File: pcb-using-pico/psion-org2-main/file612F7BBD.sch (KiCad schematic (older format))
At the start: 39 parts, among them SW1 AC_ON, SW10 n, SW11 t, SW12 del, SW13 up, SW14 c, SW15 i, SW16 o, SW17 u, SW18 y, SW19 down, SW2 A, SW20 d, SW21 j, SW22 p, SW23 v, SW24 z, SW25 left, SW26 e, SW27 k, SW28 q, SW29 w, SW3 g, SW30 spc, SW31 right, SW32 f, SW33 L, SW34 r, SW35 x, SW36 exe, SW4 m, SW5 s, SW6 shft, SW7 mode, SW8 b, SW9 h

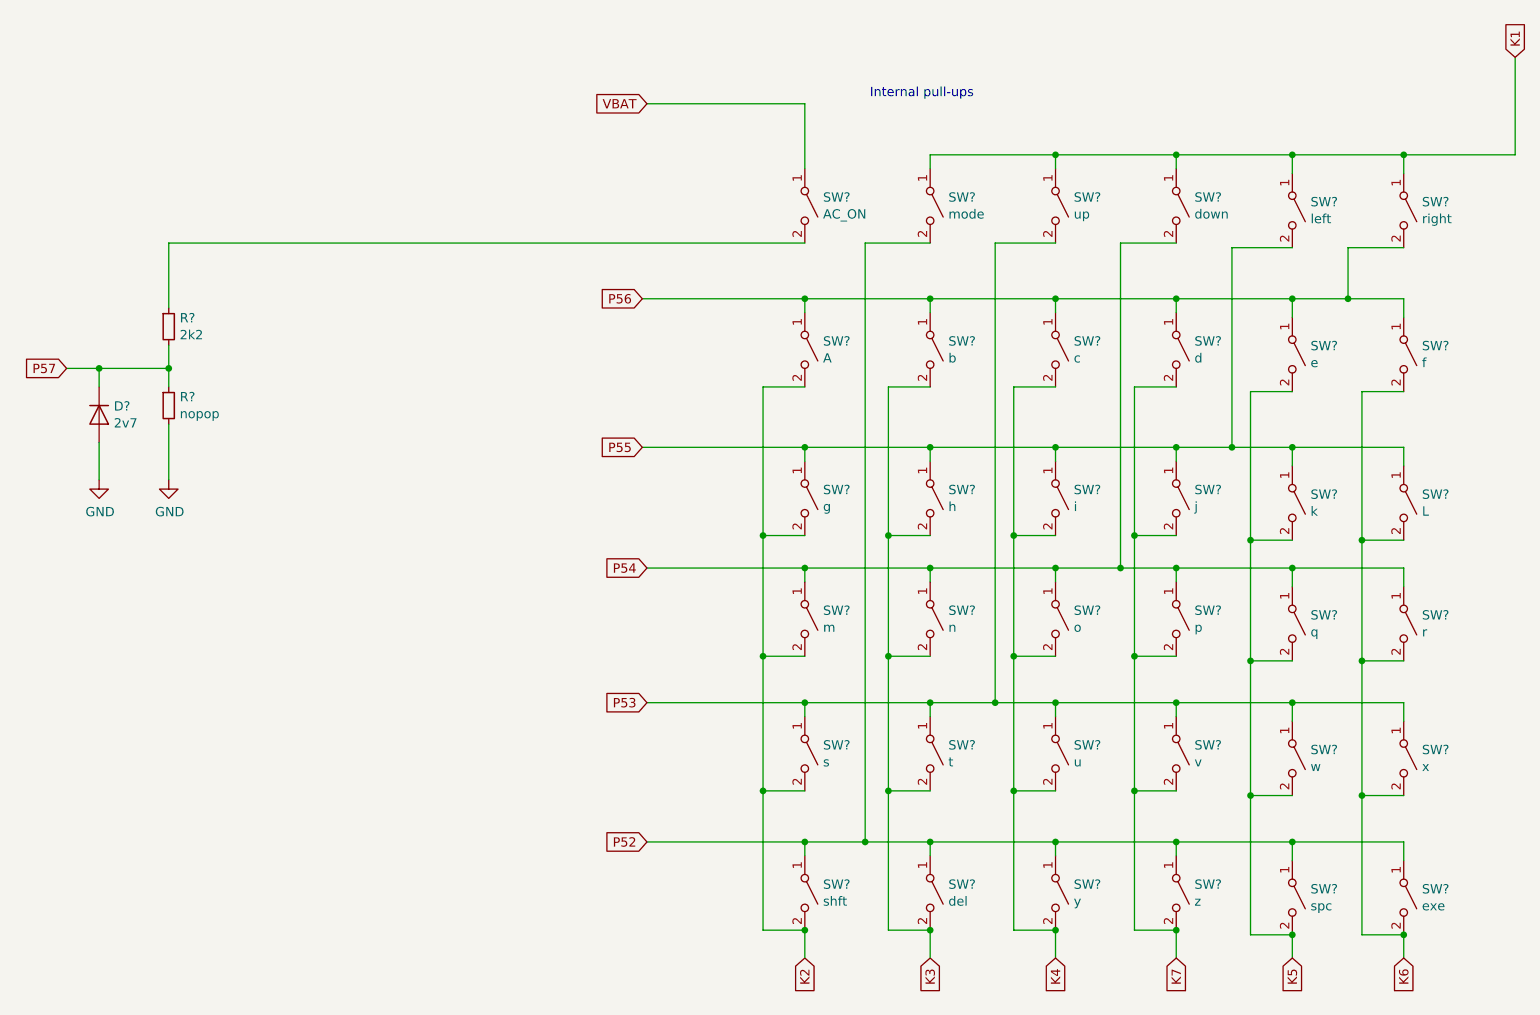
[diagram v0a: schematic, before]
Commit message: Fixed comment typo. Reverted schematic to previous version (966dcfb2f9e5fb2f0f6e9c85d958500d25748731) as a change (7bf7705c572b4e37423d66cfa6dac4b195edf464) somehow managed to create a bad hierarchical page reference for the keypad. Component designations were lost and the PCB didn't update properly. I think its all fixed now, the PCB is updated and DRC runs fine.
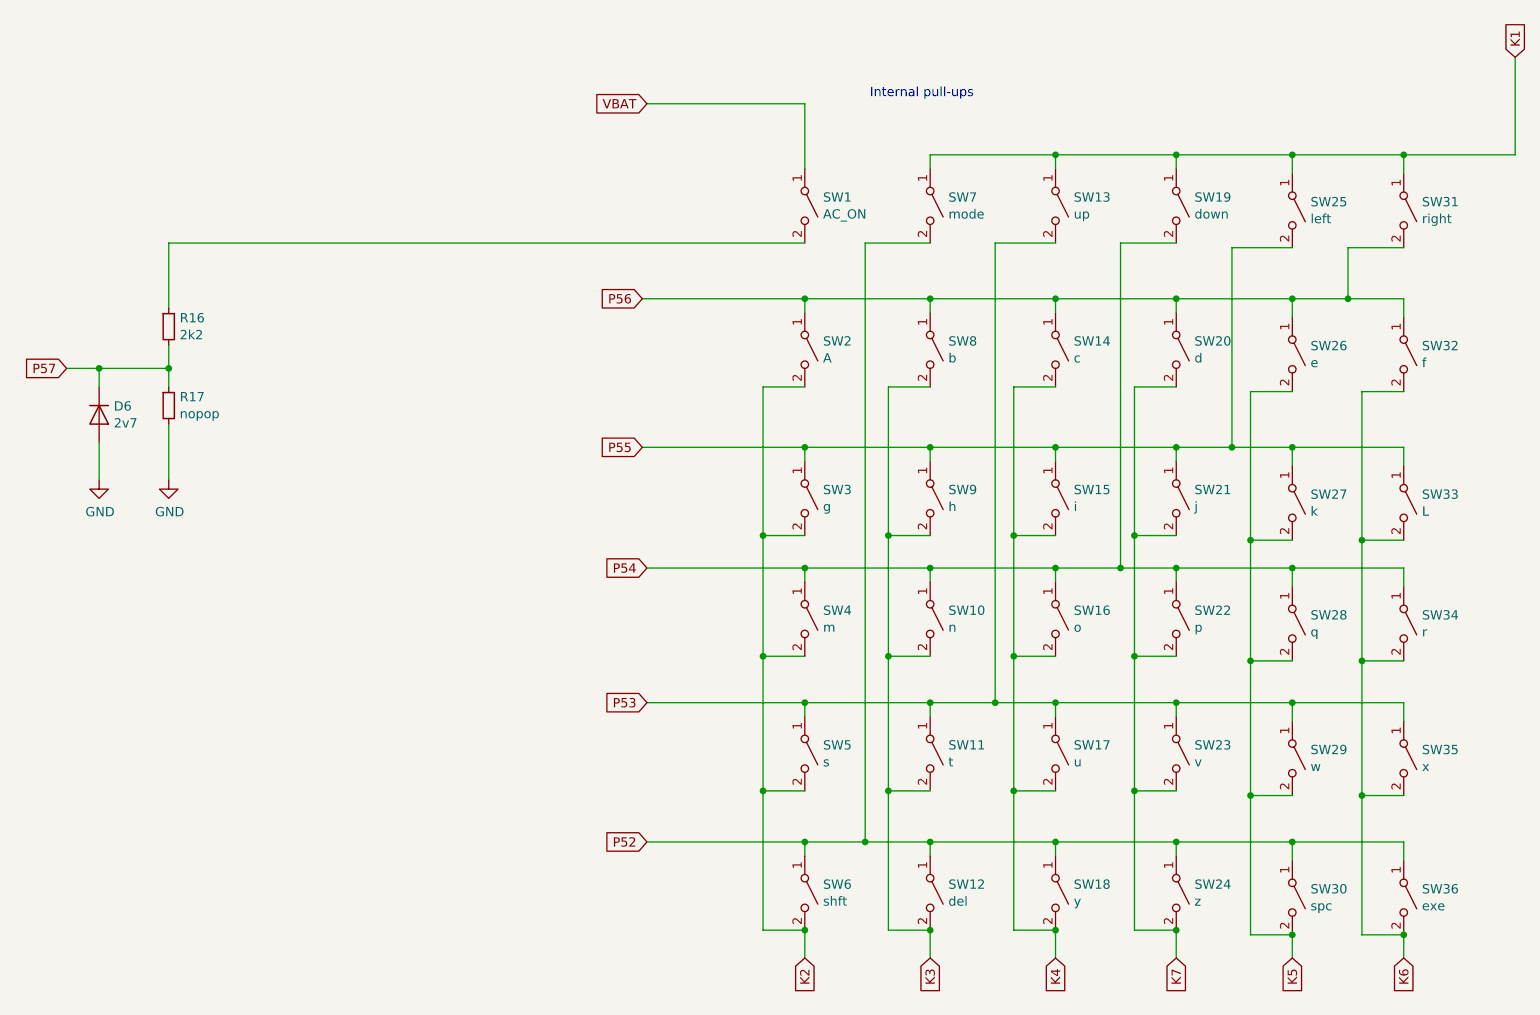
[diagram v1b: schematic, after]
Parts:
- gave numbers to parts that had none: 3
